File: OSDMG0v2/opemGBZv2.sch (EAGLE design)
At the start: 46 parts, among them IC1 TP4056, J1 SJ2-35954D-SMT-TR, SW0 WIREPADSMD1,27-254, SW1 WIREPADSMD1,27-254, U1 FS8205, U2 FS312F-G, U3 MT3608

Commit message: Update
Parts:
- removed C4: 0.1uF, rcl:C-EUC0603
- removed D1: (no value), diode:SCHOTTKY-DIODESMD
- removed IC1: TP4056, TP4056:TP4056
- removed JP3, JP4: (no value), pinhead:PINHD-1X2
- removed L1: DR74-220-R, DR74-220-R:DR74-220-R
- removed LEDG, LEDR: (no value), led:LEDCHIP-LED0603
- removed R7: 2k, rcl:R-EU_R0603
- removed SW0, SW1: WIREPADSMD1,27-254, wirepad:WIREPADSMD1,27-254
- removed U1: FS8205, fs8205:FS8205
- removed U2: FS312F-G, fs321f-g:FS312F-G
- removed USBC: 1-2295018-2, 1-2295018-2:1-2295018-2
- added 12K, 23K, R16: 205k, rcl:R-EU_R0603
- added 5V-B, GND-B, RESET, SW2, SW3: WIREPADSMD1,27-254, wirepad:WIREPADSMD1,27-254
- added BF998E6327HTSA1: INF-SOT143-4-1_V_1, INF-SOT143-4-1_V:INF-SOT143-4-1_V_1
- added C10: 33uF, rcl:C-EUC1812
- added C7: 10pF, rcl:C-EUC1812
- added C8: 10uF, rcl:C-EUC1812
- added C9: 10nF, rcl:C-EUC1812
- added IC2: TP4056, TP4056:TP4056
- added JP1: (no value), pinhead:PINHD-1X2
- added L2: 1uH, DR74-220-R:DR74-220-R
- added LEDG1, LEDR1: (no value), led:LEDCHIP-LED0603
- added MMBT9015C: INF-SOT23_M_1, INF-SOT23_M:INF-SOT23_M_1
- added R12, R8: 2k, rcl:R-EU_R0603
- added R13, R14: 1M, rcl:R-EU_R0603
- added R15: 30.9k, rcl:R-EU_R0603
- added R17: 619k, rcl:R-EU_R0603
- added R9: 100, rcl:R-EU_R0603
- added T1: BC846S, nxp_60:BC846S
- added U$3: TPS61235RWLR, CONV_TPS61235RWLR:CONV_TPS61235RWLR
- added U4: FS8205, fs8205:FS8205
- added USBC1: 1-2295018-2, 1-2295018-2:1-2295018-2
- C1: value 22uF -> 10u; device rcl:C-EUC1812 -> rcl:C-EUC0603
- C2: value 22uF -> 0.1uF; device rcl:C-EUC1812 -> rcl:C-EUC0603
- C3: value 10u -> 100uF; device rcl:C-EUC0603 -> rcl:C-EUC1812
- R1, R4: value 1k -> 150k
- R2, R3: value (none) -> 1k
- R5: value 2k -> 1k
- R6: value 100 -> 1k
- U3: value MT3608 -> FS312F-G; device mt3608:MT3608 -> fs321f-g:FS312F-G
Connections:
- removed net L-OUT1: SW0.P
- new net N$31: IC2.CHRG, R3.2
- new net N$32: LEDG1.C, R2.1
- new net N$33: L2.2, U$3.BW
- new net N$34: LEDR1.C, R3.1
- new net N$35: C7.2, R16.2, R17.1, U$3.FB
- new net N$36: IC2.PROG, R8.2
- new net N$37: U3.OC, U4.G2
- new net N$38: U3.OD, U4.G1
- new net N$39: R12.2, U3.CS
- new net N$40: 12K.1, 23K.2, RESET.P
- new net VCC: C2.2, R9.1, U3.VCC
- net 5V: now also 5V-B.P, C10.1, C3.1, C7.1, MMBT9015C.1, R1.2, R17.2, SW2.P, T1-2.C, U$3.VOUT; no longer C2.1, D1.C, JP4.1, R2.2
- net BAT+: now also C8.1, IC2.BAT, L2.1, R13.2, R14.2, R9.2, U$3.EN, U$3.VIN; no longer C1.1, IC1.BAT, L1.2, R6.2, SW1.P, U3.EN, U3.IN
- net BAT-: now also C2.1, U3.GND, U4.S1; no longer C4.1, U1.S1, U2.GND
- net GND: now also 23K.1, BF998E6327HTSA1.4, C10.2, C8.2, C9.2, IC2.GND, IC2.TEMP, R12.1, R14.1, R15.1, R16.1, R8.1, T1-1.E, U$3.AGND, U$3.PGND, U4.S2, USBC1.GND@1, USBC1.GND@2, USBC1.GND@3, USBC1.GND@4; no longer C2.2, C3.2, IC1.GND, IC1.TEMP, JP4.2, R3.1, R5.1, R7.1, U1.S2, U3.GND, USBC.GND@1, USBC.GND@2, USBC.GND@3, USBC.GND@4
- net N$11: now also BF998E6327HTSA1.1, GND-B.P; no longer IC1.STDBY, R1.2
- net N$12: now also BF998E6327HTSA1.3, MMBT9015C.3; no longer IC1.CHRG, R4.2
- net N$13: now also MMBT9015C.2, R4.2; no longer LEDG.C, R1.1
- net N$14: now also 12K.2, T1-2.E; no longer LEDR.C, R4.1
- net N$15: now also C3.2, R1.1, R4.1, T1-1.C; no longer IC1.PROG, R5.2
- net N$16: now also R6.1, T1-1.B; no longer U1.G2, U2.OC
- net N$17: now also R5.2, R6.2, SW3.P; no longer U1.G1, U2.OD
- net N$18: now also R5.1, T1-2.B; no longer R7.2, U2.CS
- net N$19: now also R13.1, U$3.INACT; no longer D1.A, L1.1, U3.SW
- net N$20: now also C9.1, R15.2, U$3.CC; no longer R2.1, R3.2, U3.FB
- net N$30: now also IC2.STDBY, R2.2; no longer C4.2, R6.1, U2.VCC
- net VBUS: now also C1.1, IC2.CE, IC2.VCC, LEDG1.A, LEDR1.A, USBC1.VBUS@1, USBC1.VBUS@2, USBC1.VBUS@3, USBC1.VBUS@4; no longer C3.1, IC1.CE, IC1.VCC, LEDG.A, LEDR.A, USBC.VBUS@1, USBC.VBUS@2, USBC.VBUS@3, USBC.VBUS@4
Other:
- note added: "AUDIO-Circuit"
- note added: "BOOST-Circuit"
- note added: "BUTTON-Circuit"
- note added: "CHARGING-Circuit"
- note added: "PROTECTION-Circuit"
- note added: "SAFE-SHUTDOWN-Circuit"
- note added: "USB-C"

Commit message: update board
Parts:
- removed JP2: (no value), pinhead:PINHD-1X13
- added C11, C12: 18pF, adafruit:C-USC0805K
- added C13, C14, C4, C5: 0.1uF, adafruit:C-USC0805K
- added C6: 10uF, adafruit:CPOL-USA/3216-18R
- added IC1: ATMEGA32U4-AU, adaprog:ATMEGA32U4-AU
- added JP3, JP4: (no value), pinhead:PINHD-1X2
- added PWR: GREEN, adafruit:LEDCHIPLED_0805
- added R18, R7: 22, rcl:R-EU_R0603
- added R19: 1k, rcl:R-EU_R0603
- added RPI-D+, RPI-D-: WIREPADSMD1,27-254, wirepad:WIREPADSMD1,27-254
- added S2: JS202011SCQN, JS202011SCQN:JS202011SCQN
- added SJ2: VCC, jumper:SJ
- added X3: 16MHz, adaprog:XTALNX5032
- renumbered U4 to U1
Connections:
- removed net N$10: JP2.11, Y.P$2
- removed net N$3: DOWN.P$2, JP2.4
- removed net N$4: JP2.5, RIGHT.P$2
- removed net N$5: JP2.6, SELECT.P$1
- removed net N$6: JP2.7, START.P$1
- removed net N$7: B.P$2, JP2.8
- removed net N$8: A.P$2, JP2.9
- removed net N$9: JP2.10, X.P$2
- new net +3V3: C4.1, IC1.UCAP
- new net A0/D18: IC1.PF7(ADC7(TDI), START.P$1
- new net A1/D19: IC1.PF6(ADC6/TDO), SELECT.P$1
- new net A11/D12: IC1.PD6(T1/OC4D/ADC9)
- new net A2/D20: IC1.PF5(ADC5/TMS)
- new net A3/D21: IC1.PF4(ADC4/TCK)
- new net A4/D22: IC1.PF1(ADC1)
- new net A5/D23: IC1.PF0(ADC0)
- new net A6/D4: IC1.PD4(ICP1/ADC8)
- new net A7/D6: IC1.PD7(OC4D/ADC10/T0), JP3.2
- new net AREF: IC1.AREF
- new net AT-D+: R18.2, S2.2
- new net AT-D-: R7.2, S2.5
- new net D+: S2.1, USBC1.D+, USBC1.D+@1
- new net D-: S2.4, USBC1.D-, USBC1.D-@1
- new net D0: IC1.PD2(INT2/RXD1)
- new net D1: IC1.PD3(INT3/TXD1)
- new net D10/A10: IC1.PB6(OC1B/OC4B/ADC13)
- new net D11: IC1.PB7(OC0A/OC1C/RTS)
- new net D13: IC1.PC7(ICP3/CLK0/OC4A)
- new net D14: A.P$2, IC1.PB3(PDO/MISO)
- new net D15: IC1.PB1(SCK)
- new net D16: B.P$2, IC1.PB2(PDI/MISO)
- new net D17: IC1.PB0(SS)
- new net D2: IC1.PD1(INT1/SDA), UP.P$2
- new net D3: IC1.PD0(INT0/OC0B), LEFT.P$2
- new net D4: DOWN.P$2
- new net D5: IC1.PC6(OC1A), RIGHT.P$2
- new net D7: IC1.PE6, JP3.1
- new net D8/A8: IC1.PB4(ADC11), Y.P$2
- new net D9/A10: IC1.PB5(OC1A/OC4B/ADC12), X.P$2
- new net N$41: IC1.D-, R7.1
- new net N$42: IC1.D+, R18.1
- new net N$43: C12.1, IC1.XTAL2, X3.P$1
- new net N$44: C11.1, IC1.XTAL1, X3.P$2
- new net N$45: PWR.A, R19.2
- net 5V: now also C5.1, C6.+, IC1.UVCC, IC1.VBUS, R19.1, SJ2.2
- net GND: now also C11.2, C12.2, C13.2, C14.2, C4.2, C5.2, C6.-, IC1.GND, IC1.GND1, IC1.GND2, IC1.GND3, IC1.UGND, PWR.C; no longer JP2.1
- net L-OUT: now also JP4.1; no longer JP2.12
- net N$1: now also RPI-D-.P, S2.6; no longer JP2.2, LEFT.P$2
- net N$2: now also RPI-D+.P, S2.3; no longer JP2.3, UP.P$2
- net R-OUT: now also JP4.2; no longer JP2.13
- net VCC: now also C13.1, C14.1, IC1.AVCC, IC1.AVCC1, IC1.VCC, IC1.VCC1, SJ2.1
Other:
- note added: "1P Start"
- note added: "Coin/Credit"
- note added: "Enter"
- note added: "Key-Down"
- note added: "Key-Left"
- note added: "Key-Right"
- note added: "Key-UP"
- note added: "Left-Alt"
- note added: "Left-Ctrl"
- note added: "Left-Shift"
- note added: "Spacebar"
- note added: "Z"
- moved on the sheet: JP1, USBC1

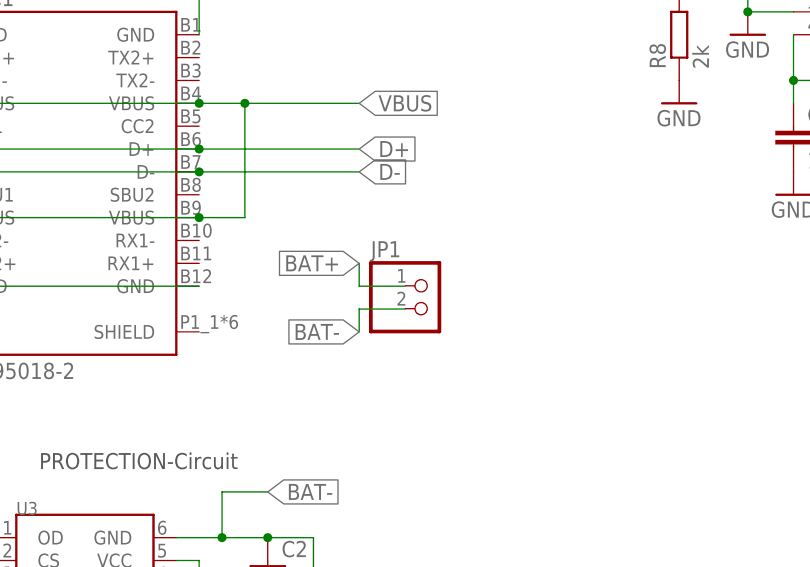
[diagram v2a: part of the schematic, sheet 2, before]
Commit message: everything routed up GND
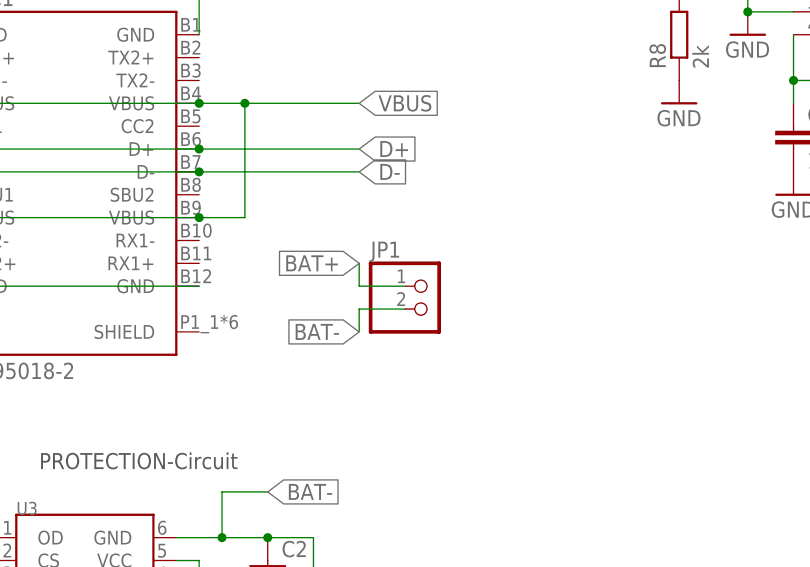
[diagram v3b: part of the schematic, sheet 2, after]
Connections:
- net BAT+: now also JP1.1
- net BAT-: now also JP1.2
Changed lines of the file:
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@@
 <part name="P+2" library="supply1" deviceset="VCC" device=""/>
 <part name="USBC1" library="1-2295018-2" deviceset="1-2295018-2" device=""/>
-<part name="JP1" library="pinhead" library_urn="urn:adsk.eagle:library:325" deviceset="PINHD-1X2" device="" package3d_urn="urn:adsk.eagle:package:22435/2"/>
 <part name="R19" library="rcl" library_urn="urn:adsk.eagle:library:334" deviceset="R-EU_" device="R0603" package3d_urn="urn:adsk.eagle:package:23555/2" value="1k"/>
 <part name="R18" library="rcl" library_urn="urn:adsk.eagle:library:334" deviceset="R-EU_" device="R0603" package3d_urn="urn:adsk.eagle:package:23555/2" value="22"/>
@@
 <part name="U$1" library="diy-modules" deviceset="AMPLIFIER-PAM8403" device=""/>
 <part name="U1" library="fs8205" deviceset="FS8205" device=""/>
+<part name="JP1" library="pinhead" library_urn="urn:adsk.eagle:library:325" deviceset="PINHD-1X2" device="" package3d_urn="urn:adsk.eagle:package:22435/2"/>
 </parts>
 <sheets>
@@
 <instance part="RESET" gate="G$1" x="368.3" y="7.62" rot="R180"/>
 <instance part="USBC1" gate="G$1" x="111.76" y="81.28"/>
-<instance part="JP1" gate="G$1" x="152.422603125" y="66.084984375"/>
 <instance part="U1" gate="U1" x="121.92" y="12.7" rot="R270"/>
+<instance part="JP1" gate="G$1" x="152.4" y="66.04"/>
 </instances>
 <busses>
@@
 <wire x1="144.78" y1="68.58" x2="144.78" y2="71.12" width="0.1524" layer="91"/>
 <wire x1="149.86" y1="68.58" x2="144.78" y2="68.58" width="0.1524" layer="91"/>
+<pinref part="JP1" gate="G$1" pin="1"/>
 </segment>
 </net>
@@
 <wire x1="144.78" y1="66.04" x2="144.78" y2="63.5" width="0.1524" layer="91"/>
 <wire x1="149.86" y1="66.04" x2="144.78" y2="66.04" width="0.1524" layer="91"/>
-</segment>
-</net>
+<pinref part="JP1" gate="G$1" pin="2"/>
+</segment>
+</net>
